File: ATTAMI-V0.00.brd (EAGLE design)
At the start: 22.8 x 22.9 mm, 24 parts, among them U1 MIC5225, U2 ATTINY85

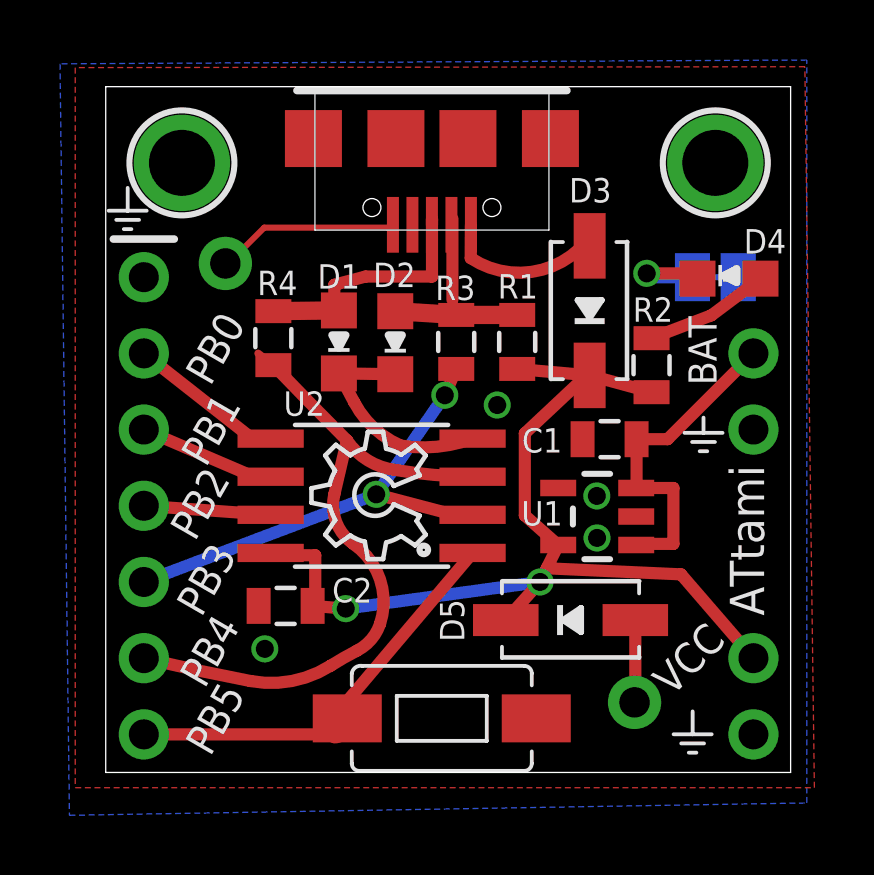
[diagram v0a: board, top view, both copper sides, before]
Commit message: removed unuised ID pin from micro usb connector
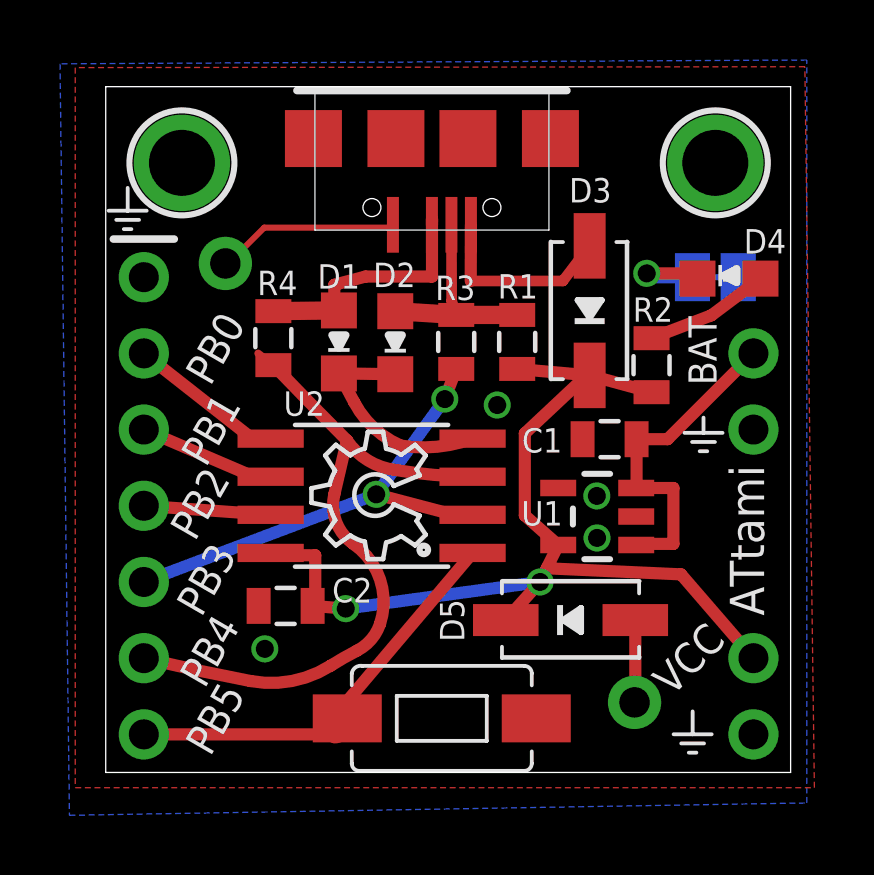
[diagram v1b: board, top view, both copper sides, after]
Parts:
- USB: device yair_r:USB-MICRO-ALIEXPRESS -> ATtami:USB-MICRO-ALIEXPRESS
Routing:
- net V-BUS: track 5.19 -> 6.60 mm
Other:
- board text added: "V 0.00"

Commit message: moved all parts to ATtami lib, trimmed it
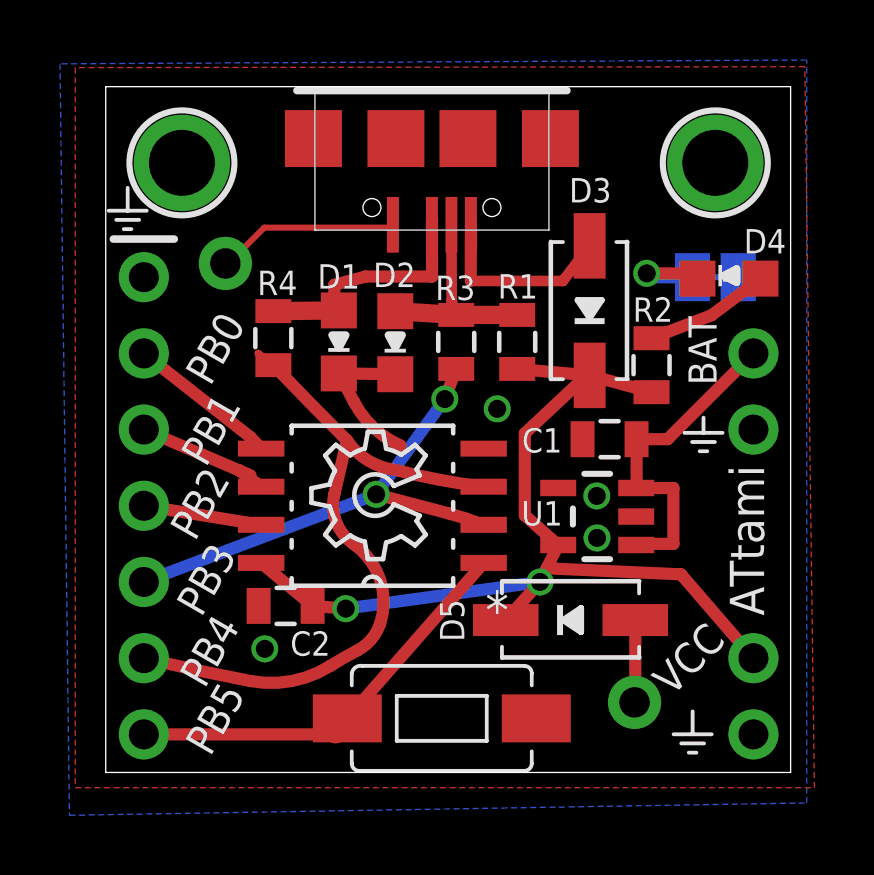
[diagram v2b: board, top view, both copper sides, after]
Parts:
- C1, C2, R1, R2, R3, R4: device SparkFun:0805 -> ATtami:0805
- COIN_CELL_(+), COIN_CELL_(-): device adafruit:1X01-CLEANBIG -> ATtami:1X01-CLEANBIG
- D1, D2, D4: device dp_devices:LED-805 -> ATtami:LED-805
- D3, D5: device microbuilder:SOD-323 -> ATtami:SOD-323
- J1: device microbuilder:1X07_ROUND -> ATtami:1X07_ROUND
- J2, J3: device microbuilder:1X02_ROUND -> ATtami:1X02_ROUND
- S1: device SparkFun-Electromechanical:TACTILE-SWITCH-1101NE -> ATtami:TACTILE-SWITCH-1101NE
- SJ1: device microbuilder:SOLDERJUMPER_CLOSEDWIRE -> ATtami:SOLDERJUMPER_CLOSEDWIRE
- U$1, U$2: device microbuilder:MOUNTINGHOLE_2.0_PLATED -> ATtami:MOUNTINGHOLE_2.0_PLATED
- U1: device SparkFun:SOT23-5 -> ATtami:SOT23-5
- U2: value ATTINY85 -> ATTINY85-20SU; device SparkFun:SO08-EIAJ -> ATtami:SOIC127P798X216-8N
- moved U2 0.34 mm to (8.89, 8.89), turned to 180 degrees
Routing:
- net GND: track 13.6 -> 11.2 mm
- net VCC: track 35.2 -> 32.8 mm
- net PB5: track 15.0 -> 13.9 mm

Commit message: updated layout
including re-routing the EN-VIN connection on U1 and removing a few
routes that allows for this design to work as a one layer board with a
bit of work.
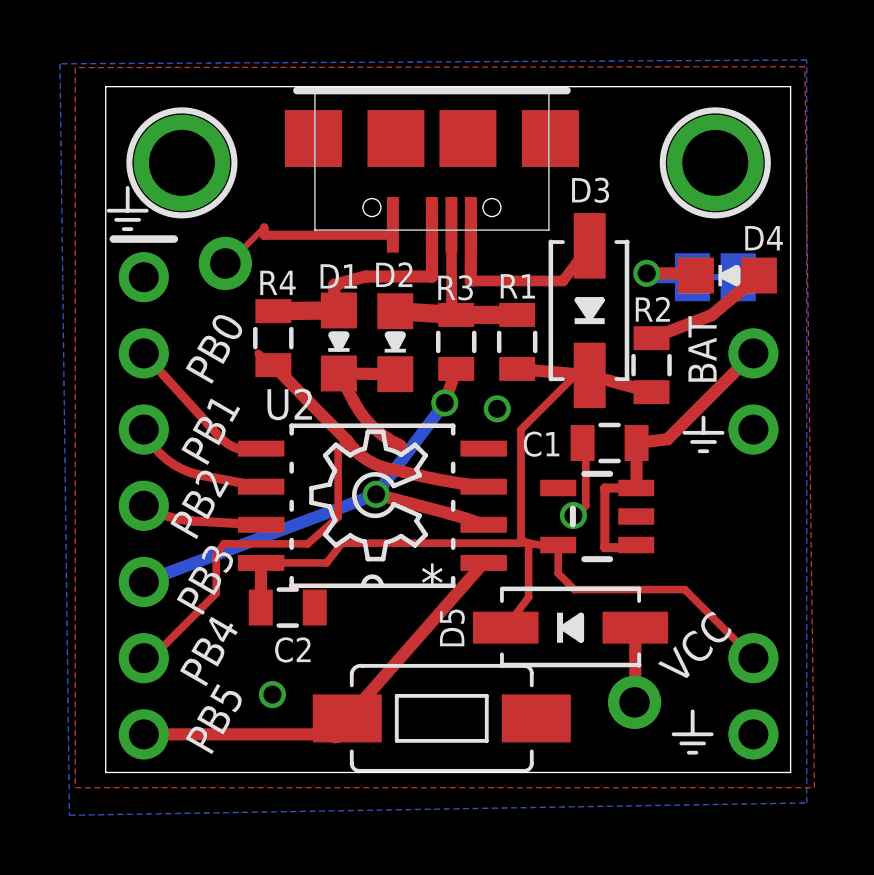
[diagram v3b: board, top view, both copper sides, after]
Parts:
- moved D5 0.25 mm to (15.5, 4.83)
- moved C1 0.13 mm to (16.8, 11.0)
- moved D4 0.11 mm to (20.7, 16.6)
- moved C2 0.09 mm to (6.07, 5.50), turned to 0 degrees
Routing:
- net GND: track 11.2 -> 14.4 mm, vias 4 -> 3
- net PB4: track 24.0 -> 20.9 mm
- net VCC: track 32.8 -> 35.0 mm, vias 2 -> 0
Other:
- board text removed: "ATtami"

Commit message: small layout change
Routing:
- net GND: track 14.4 -> 11.2 mm
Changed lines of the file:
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@@
 <wire x1="7.7724" y1="13.301" x2="9.652" y2="13.2756" width="0.4064" layer="1"/>
 <via x="13.05051875" y="12.120878125" extent="1-16" drill="0.6"/>
-<wire x1="7.7724" y1="13.301" x2="8.2804" y2="12.3444" width="0.4064" layer="1"/>
-<wire x1="8.2804" y1="12.3444" x2="9.8298" y2="10.8966" width="0.4064" layer="1" curve="38.525939"/>
 <contactref element="J1" pad="1"/>
 <via x="5.55751875" y="2.595878125" extent="1-16" drill="0.6"/>

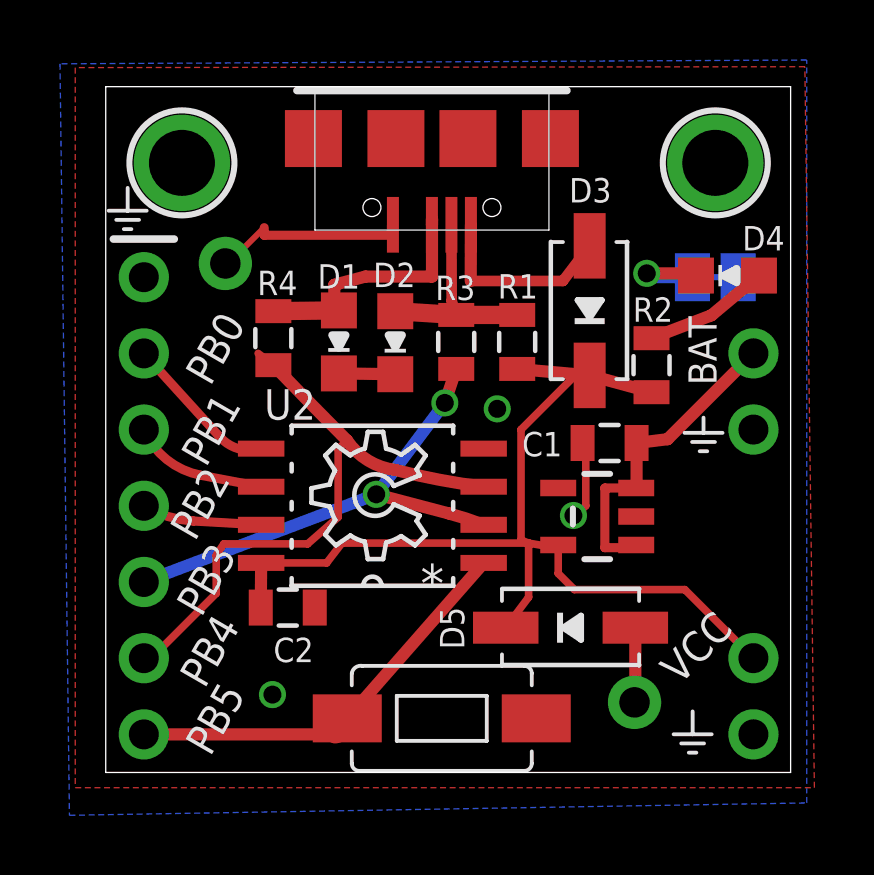
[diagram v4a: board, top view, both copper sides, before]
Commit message: re introduced the vias under the regulator
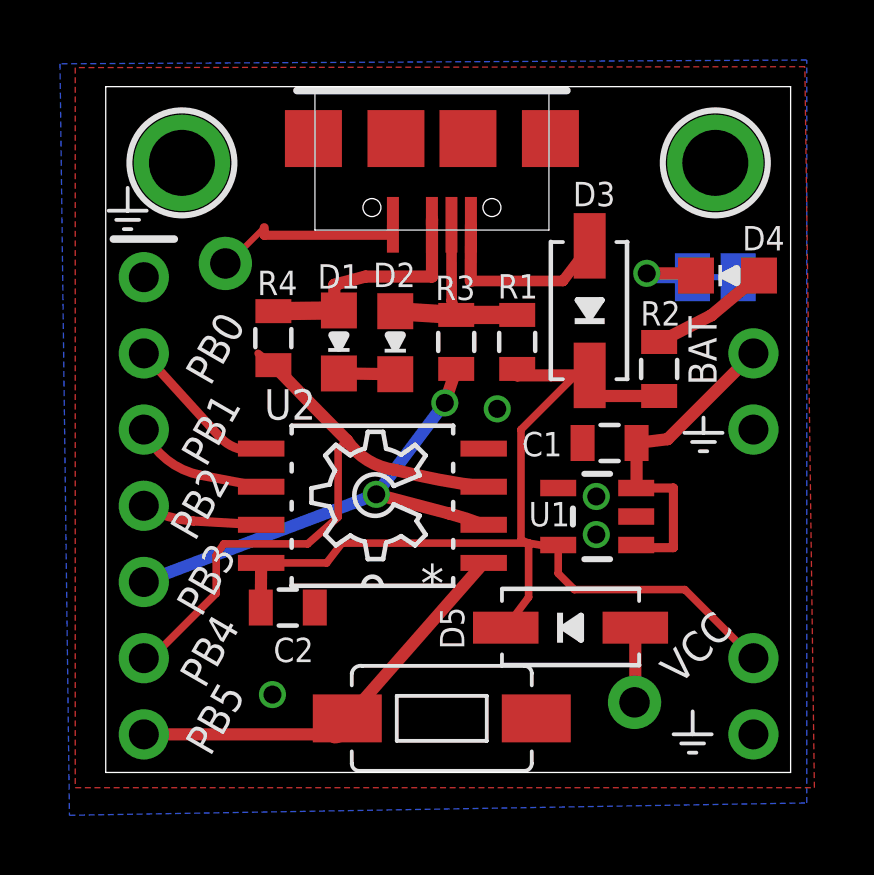
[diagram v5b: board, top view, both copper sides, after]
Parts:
- moved R2 0.28 mm to (18.4, 13.4)
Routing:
- net GND: track 11.2 -> 8.55 mm, vias 3 -> 4
- net VCC: track 35.0 -> 36.1 mm
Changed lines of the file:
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@@
 </element>
 <element name="D3" library="ATtami" package="SOD-323" value="Schottky" x="16.1315375" y="15.394940625" smashed="yes" rot="R90">
-<attribute name="NAME" x="16.858159375" y="19.812759375" size="0.8128" layer="25" font="vector" ratio="18" rot="R180"/>
+<attribute name="NAME" x="16.985159375" y="19.685759375" size="0.8128" layer="25" font="vector" ratio="18" rot="R180"/>
 </element>
 <element name="C2" library="ATtami" package="0805" value="2.2uf/16V" x="6.068059375" y="5.496559375" smashed="yes">
@@
 <attribute name="VALUE" x="21.9949875" y="19.103753125" size="1.27" layer="27" ratio="10" rot="R180" display="off"/>
 </element>
-<element name="R2" library="ATtami" package="0805" value="1K5" x="18.194021875" y="13.5763" smashed="yes" rot="R270">
-<attribute name="NAME" x="17.571721875" y="15.0241" size="0.8128" layer="25"/>
-<attribute name="VALUE" x="16.797021875" y="14.5923" size="0.4064" layer="27" rot="R270" display="off"/>
-</element>
-<element name="U1" library="ATtami" package="SOT23-5" value="MIC5225" x="16.383003125" y="8.5318625" smashed="yes" rot="R90"/>
+<element name="R2" library="ATtami" package="0805" value="1K5" x="18.448021875" y="13.4493" smashed="yes" rot="R270">
+<attribute name="NAME" x="17.825721875" y="14.8971" size="0.8128" layer="25"/>
+<attribute name="VALUE" x="17.051021875" y="14.4653" size="0.4064" layer="27" rot="R270" display="off"/>
+</element>
+<element name="U1" library="ATtami" package="SOT23-5" value="MIC5225" x="16.383003125" y="8.5318625" smashed="yes" rot="R90">
+<attribute name="NAME" x="15.4711375" y="9.017003125" size="0.8128" layer="25" rot="R180"/>
+<attribute name="VALUE" x="16.573503125" y="7.5793625" size="0.4064" layer="27" rot="R90"/>
+</element>
 <element name="U$1" library="ATtami" package="MOUNTINGHOLE_2.0_PLATED" value="MOUNTINGHOLE2.0" x="2.54" y="20.32" smashed="yes" rot="R270"/>
 <element name="S1" library="ATtami" package="TACTILE-SWITCH-1101NE" value="SWITCH-MOMENTARY-2-SMD-1101NE" x="11.2014" y="1.8034" smashed="yes" rot="R180">
@@
 </element>
 <element name="D5" library="ATtami" package="SOD-323" value="Schottky" x="15.494" y="4.826" smashed="yes">
-<attribute name="NAME" x="11.954" y="4.107" size="0.8128" layer="25" ratio="18" rot="R90"/>
+<attribute name="NAME" x="11.954" y="4.107" size="0.8128" layer="25" font="vector" ratio="18" rot="R90"/>
 <attribute name="VALUE" x="13.251" y="2.78" size="0.4064" layer="27" ratio="10" display="off"/>
 </element>
@@
 <wire x1="4.1275" y1="17.0053" x2="3.9878" y2="16.9672" width="0.2032" layer="1"/>
 <contactref element="U2" pad="4"/>
-<via x="15.59051875" y="8.564878125" extent="1-16" drill="0.6"/>
-<wire x1="15.59051875" y1="8.564878125" x2="15.676878125" y2="8.564878125" width="0.254" layer="1"/>
-<wire x1="15.676878125" y1="8.564878125" x2="16.002" y2="8.89" width="0.254" layer="1"/>
-<wire x1="16.002" y1="8.89" x2="16.002" y2="10.875440625" width="0.254" layer="1"/>
-<wire x1="16.002" y1="10.875440625" x2="15.89538125" y2="10.982059375" width="0.254" layer="1"/>
 <wire x1="9.573740625" y1="18.2553" x2="9.525" y2="18.2553" width="0.3048" layer="1"/>
 <wire x1="9.525" y1="18.2553" x2="9.525" y2="17.907" width="0.3048" layer="1"/>
 <wire x1="9.525" y1="17.907" x2="5.2832" y2="17.907" width="0.3048" layer="1"/>
 <wire x1="5.2832" y1="17.907" x2="5.2832" y2="18.161" width="0.3048" layer="1"/>
+<via x="16.35251875" y="9.199878125" extent="1-16" drill="0.6"/>
+<via x="16.35251875" y="7.929878125" extent="1-16" drill="0.6"/>
 </signal>
 <signal name="PB3">
@@
 <wire x1="17.69538125" y1="10.982059375" x2="18.729059375" y2="11.109059375" width="0.4064" layer="1"/>
 <wire x1="18.729059375" y1="11.109059375" x2="21.59" y2="13.97" width="0.4064" layer="1"/>
-<wire x1="17.683103125" y1="9.4818625" x2="16.637" y2="9.4818625" width="0.3048" layer="1"/>
-<wire x1="16.637" y1="9.4818625" x2="16.637" y2="7.493" width="0.3048" layer="1"/>
-<wire x1="16.637" y1="7.493" x2="17.683103125" y2="7.493" width="0.3048" layer="1"/>
+<wire x1="17.683103125" y1="9.4818625" x2="18.923" y2="9.4818625" width="0.3048" layer="1"/>
+<wire x1="18.923" y1="9.4818625" x2="18.923" y2="7.493" width="0.3048" layer="1"/>
+<wire x1="18.923" y1="7.493" x2="17.683103125" y2="7.493" width="0.3048" layer="1"/>
 <wire x1="17.683103125" y1="7.493" x2="17.683103125" y2="7.5818625" width="0.3048" layer="1"/>
 </signal>
@@
 <contactref element="D5" pad="CQ"/>
 <contactref element="J3" pad="1"/>
-<wire x1="18.194021875" y1="12.6763" x2="16.1315375" y2="13.235940625" width="0.4064" layer="1"/>
-<wire x1="13.716" y1="13.451" x2="16.1315375" y2="13.235940625" width="0.4064" layer="1"/>
 <contactref element="U2" pad="8"/>
 <wire x1="5.1816" y1="6.985" x2="5.168059375" y2="5.496559375" width="0.4064" layer="1"/>
@@
 <wire x1="15.621" y1="6.096" x2="19.304" y2="6.096" width="0.254" layer="1"/>
 <wire x1="19.304" y1="6.096" x2="21.59" y2="3.81" width="0.254" layer="1"/>
+<wire x1="18.448021875" y1="12.5493" x2="16.129" y2="12.5493" width="0.4064" layer="1"/>
+<wire x1="16.129" y1="12.5493" x2="16.129" y2="12.573" width="0.4064" layer="1"/>
+<wire x1="16.129" y1="12.573" x2="16.1315375" y2="12.573" width="0.4064" layer="1"/>
+<wire x1="16.1315375" y1="12.573" x2="16.1315375" y2="13.235940625" width="0.4064" layer="1"/>
+<wire x1="16.1315375" y1="13.235940625" x2="13.716" y2="13.235940625" width="0.4064" layer="1"/>
+<wire x1="13.716" y1="13.235940625" x2="13.716" y2="13.451" width="0.4064" layer="1"/>
 </signal>
 <signal name="PB1">
@@
 <contactref element="R2" pad="1"/>
 <contactref element="D4" pad="A"/>
-<wire x1="18.194021875" y1="14.4763" x2="20.193" y2="15.24" width="0.4064" layer="1"/>
+<wire x1="18.448021875" y1="14.3493" x2="20.193" y2="15.24" width="0.4064" layer="1"/>
 <wire x1="20.193" y1="15.24" x2="21.7749875" y2="16.563753125" width="0.4064" layer="1"/>
 </signal>
